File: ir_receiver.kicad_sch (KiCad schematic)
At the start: 15 parts

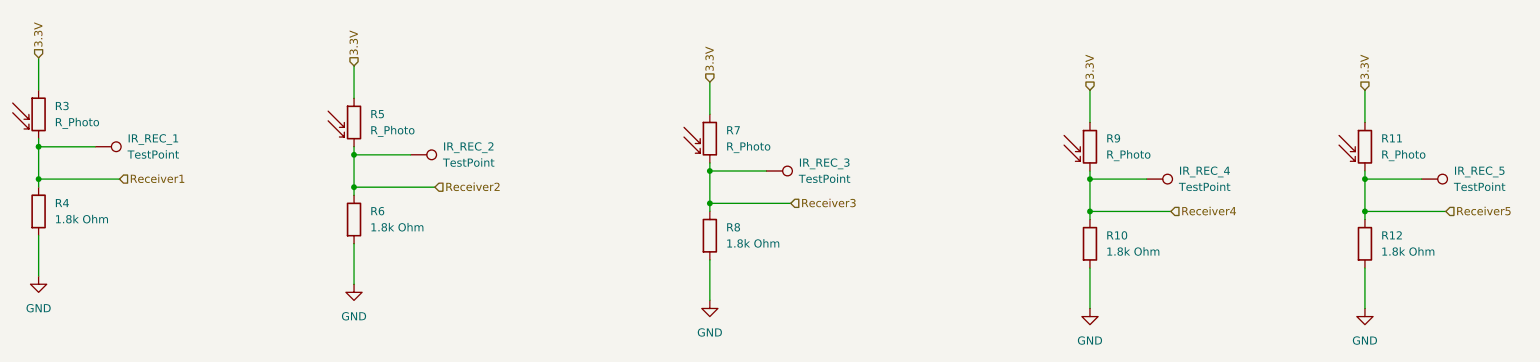
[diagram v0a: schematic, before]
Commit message: pcb: all wired up, most warnings can't be fixed.
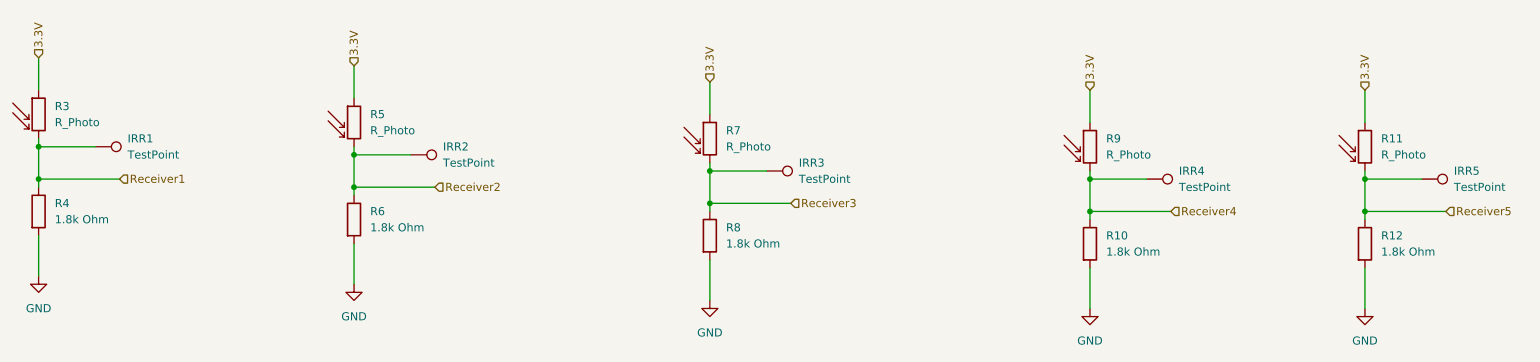
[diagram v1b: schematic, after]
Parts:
- renumbered IR_REC_1 to IRR1, IR_REC_2 to IRR2, IR_REC_3 to IRR3, IR_REC_4 to IRR4, IR_REC_5 to IRR5
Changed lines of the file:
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@@
 		(dnp no)
 		(fields_autoplaced yes)
-		(property "Reference" "IR_REC_1"
+		(property "Reference" "IRR1"
 			(at 53.34 49.5299 90)
 			(effects
@@
 			(project ""
 				(path "/0ec4df52-ef34-4d49-9154-02bae5c96110/a08490c3-504f-4e44-859c-53974afb61ea"
-					(reference "IR_REC_1")
+					(reference "IRR1")
 					(unit 1)
 				)
@@
 		(dnp no)
 		(fields_autoplaced yes)
-		(property "Reference" "IR_REC_5"
+		(property "Reference" "IRR5"
 			(at 261.62 54.6099 90)
 			(effects
@@
 			(project "RoboMaus"
 				(path "/0ec4df52-ef34-4d49-9154-02bae5c96110/a08490c3-504f-4e44-859c-53974afb61ea"
-					(reference "IR_REC_5")
+					(reference "IRR5")
 					(unit 1)
 				)
@@
 		(dnp no)
 		(fields_autoplaced yes)
-		(property "Reference" "IR_REC_2"
+		(property "Reference" "IRR2"
 			(at 102.87 50.7999 90)
 			(effects
@@
 			(project "RoboMaus"
 				(path "/0ec4df52-ef34-4d49-9154-02bae5c96110/a08490c3-504f-4e44-859c-53974afb61ea"
-					(reference "IR_REC_2")
+					(reference "IRR2")
 					(unit 1)
 				)
@@
 		(dnp no)
 		(fields_autoplaced yes)
-		(property "Reference" "IR_REC_4"
+		(property "Reference" "IRR4"
 			(at 218.44 54.6099 90)
 			(effects
@@
 			(project "RoboMaus"
 				(path "/0ec4df52-ef34-4d49-9154-02bae5c96110/a08490c3-504f-4e44-859c-53974afb61ea"
-					(reference "IR_REC_4")
+					(reference "IRR4")
 					(unit 1)
 				)
@@
 		(dnp no)
 		(fields_autoplaced yes)
-		(property "Reference" "IR_REC_3"
+		(property "Reference" "IRR3"
 			(at 158.75 53.3399 90)
 			(effects
@@
 			(project "RoboMaus"
 				(path "/0ec4df52-ef34-4d49-9154-02bae5c96110/a08490c3-504f-4e44-859c-53974afb61ea"
-					(reference "IR_REC_3")
-					(unit 1)
-				)
+					(reference "IRR3")
+					(unit 1)
+				)
